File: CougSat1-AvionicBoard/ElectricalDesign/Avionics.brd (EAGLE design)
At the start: 90.4 x 95.8 mm, 214 parts, among them J1 CougSat Card, J10 IHU SD0, J11 IHU SD1, J12 IFJR SD0, J13 iFJR SD1, J14 +X Panel GPS, J15 +X, J2 -X, J3 +Z, J4 SWD, J5 +Y, J6 -Y, J7 SWD, J8 SWD, J9 -Z, U1 AD7291, U10 BNO055, U11 TXS0102DQM, U12 TXS0102DQM, U13 TXS0102DQM, U14 TXS0102DQM, U15 AD7291, U16 TXS0102DQM, U17 STM32L476RGT, U18 STM32L476RGT, U19 TXS0102DQM, U2 AD8515, U20 AD8515, U21 AD8515, U22 AD7291, U23 INA199C2, U24 AD8515, U25 DRV8837, U26 INA199C2, U27 Venus838FLPx-L, U28 DRV8837, U29 INA199C2, U3 M24M01, U30 DRV8837, U4 M24M01, U5 BNO055, U6 STM32L476RGT, U7 BNO055, U8 TXS0102DQM, U9 TXS0102DQM, Y1 32.768kHz ±10ppm, Y2 8MHz ±10ppm, Y3 32.768kHz ±10ppm, Y4 32.768kHz ±10ppm, Y5 32.768kHz ±10ppm, Y6 8MHz ±10ppm, Y7 8MHz ±10ppm, Y8 32.768kHz ±10ppm, Y9 32.768kHz ±10ppm

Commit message: Produced mCAD
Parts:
- DS1: value Yellow -> Green
- DS2: value Blue -> Green
- DS4: value Green -> Blue
- moved DS4 0.20 mm to (83.2, 4.00), flipped to the top, turned to 0 degrees
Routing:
- net 3.3V_2: track 466.7 -> 467.5 mm, vias 43 -> 44
- net GPS_LED_DIODE: track 3.69 -> 4.33 mm, vias 0 -> 1
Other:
- board text added: "Avionics V1.3"
- board text removed: "Avionics V1.1"

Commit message: new avionics update
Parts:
- added U$1: Orion B16, CougsInSpace-Boards:ORION_B16
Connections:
- new net VCC: U$1.23
- net DGND: now also U$1.10, U$1.12, U$1.13, U$1.22, U$1.24
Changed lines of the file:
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@@
 <?xml version="1.0" encoding="utf-8"?>
 <!DOCTYPE eagle SYSTEM "eagle.dtd">
-<eagle version="9.5.1">
+<eagle version="9.6.2">
 <drawing>
 <settings>
-<setting alwaysvectorfont="yes"/>
+<setting alwaysvectorfont="no"/>
 <setting verticaltext="up"/>
 </settings>
@@
 <layer number="21" name="tPlace" color="7" fill="1" visible="yes" active="yes"/>
 <layer number="22" name="bPlace" color="7" fill="1" visible="no" active="yes"/>
-<layer number="23" name="tOrigins" color="15" fill="1" visible="no" active="yes"/>
-<layer number="24" name="bOrigins" color="15" fill="1" visible="no" active="yes"/>
+<layer number="23" name="tOrigins" color="15" fill="1" visible="yes" active="yes"/>
+<layer number="24" name="bOrigins" color="15" fill="1" visible="yes" active="yes"/>
 <layer number="25" name="tNames" color="7" fill="1" visible="yes" active="yes"/>
 <layer number="26" name="bNames" color="7" fill="1" visible="no" active="yes"/>
@@
 </element>
 <element name="LOGO1" library="CougsInSpace-Aesthetics" package="SIGN-GABE" value="SIGNATUREGABE" x="87.3" y="-42.2" smashed="yes" rot="MR90"/>
+<element name="U$1" library="CougsInSpace-Boards" package="ORION_B16" value="Orion B16" x="59.6" y="-2" smashed="yes">
+<attribute name="NAME" x="59.6" y="7.1" size="0.8" layer="25" font="vector" ratio="15" align="center"/>
+<attribute name="SKU" value="03-0002" x="59.6" y="-2" size="1.778" layer="27" display="off"/>
+</element>
 </elements>
 <signals>
@@
 <wire x1="57.19" y1="-0.05" x2="55.95" y2="-1.29" width="0.2" layer="16"/>
 <wire x1="54.64" y1="-0.05" x2="54.4" y2="-0.05" width="0.2" layer="16"/>
-<wire x1="55.95" y1="-1.29" x2="55.95" y2="-1.36" width="0.2" layer="16"/>
-<wire x1="55.95" y1="-1.36" x2="55.95" y2="-1.4" width="0.2" layer="16"/>
+<wire x1="55.95" y1="-1.29" x2="55.95" y2="-1.4" width="0.2" layer="16"/>
 <via x="55.3" y="-0.89" extent="1-16" drill="0.3"/>
 <via x="52.8" y="-4.31" extent="1-16" drill="0.3"/>
@@
 <wire x1="50" y1="0" x2="55" y2="0" width="0.2" layer="2"/>
 <wire x1="55" y1="0" x2="55.3" y2="0" width="0.2" layer="2"/>
-<wire x1="55.3" y1="0" x2="55.9" y2="0" width="0.2" layer="2"/>
-<wire x1="55.9" y1="0" x2="60" y2="0" width="0.2" layer="2"/>
+<wire x1="55.3" y1="0" x2="60" y2="0" width="0.2" layer="2"/>
 <wire x1="60" y1="0" x2="65" y2="0" width="0.2" layer="2"/>
 <wire x1="65" y1="0" x2="70" y2="0" width="0.2" layer="2"/>
@@
 <wire x1="65" y1="5" x2="65" y2="10" width="0.2" layer="2"/>
 <wire x1="65" y1="10" x2="65" y2="14" width="0.2" layer="2"/>
-<wire x1="65" y1="14" x2="65" y2="16.7" width="0.2" layer="2"/>
-<wire x1="65" y1="16.7" x2="65" y2="17.9" width="0.2" layer="2"/>
+<wire x1="65" y1="14" x2="65" y2="17.9" width="0.2" layer="2"/>
 <wire x1="65" y1="17.9" x2="65" y2="21.9" width="0.2" layer="2"/>
 <wire x1="65" y1="21.9" x2="65" y2="24.9" width="0.2" layer="2"/>
@@
 <wire x1="23.835" y1="1.035" x2="23.8" y2="1" width="0.2" layer="2"/>
 <wire x1="17.6" y1="-12.9" x2="26.315" y2="-12.9" width="0.2" layer="2"/>
-<wire x1="33.62098125" y1="-12.37901875" x2="33.62098125" y2="-12.3" width="0.2" layer="2"/>
-<wire x1="33.62098125" y1="-12.3" x2="33.62098125" y2="-7.87901875" width="0.2" layer="2"/>
+<wire x1="33.62098125" y1="-12.37901875" x2="33.62098125" y2="-7.87901875" width="0.2" layer="2"/>
 <wire x1="35.5" y1="-6" x2="35.5" y2="-3.4" width="0.2" layer="2"/>
 <wire x1="33.62098125" y1="-7.87901875" x2="35.5" y2="-6" width="0.2" layer="2"/>
@@
 <wire x1="30" y1="22.505" x2="30.15" y2="22.355" width="0.2" layer="2"/>
 <wire x1="30" y1="10" x2="30" y2="11.8" width="0.2" layer="2"/>
-<wire x1="30" y1="11.8" x2="30" y2="12" width="0.2" layer="2"/>
-<wire x1="30" y1="12" x2="30" y2="13.8" width="0.2" layer="2"/>
+<wire x1="30" y1="11.8" x2="30" y2="13.8" width="0.2" layer="2"/>
 <wire x1="30" y1="13.8" x2="30" y2="22.205" width="0.2" layer="2"/>
 <wire x1="30" y1="22.205" x2="30.15" y2="22.355" width="0.2" layer="2"/>
@@
 <wire x1="35" y1="18.9" x2="35" y2="23.4" width="0.2" layer="2"/>
 <wire x1="35" y1="23.4" x2="34.7" y2="23.7" width="0.2" layer="2"/>
-<wire x1="35.465" y1="18.9" x2="35.1" y2="18.9" width="0.2" layer="2"/>
-<wire x1="35.1" y1="18.9" x2="35" y2="18.9" width="0.2" layer="2"/>
+<wire x1="35.465" y1="18.9" x2="35" y2="18.9" width="0.2" layer="2"/>
 <wire x1="34.135" y1="15.025" x2="34.975" y2="15.025" width="0.2" layer="2"/>
 <wire x1="34.975" y1="15.025" x2="35" y2="15" width="0.2" layer="2"/>
@@
 <wire x1="45" y1="14.7" x2="44.7" y2="15" width="0.2" layer="2"/>
 <wire x1="44.7" y1="15" x2="44.5" y2="15.2" width="0.2" layer="2"/>
-<wire x1="44.5" y1="17.3" x2="44.5" y2="15.2" width="0.2" layer="2"/>
 <wire x1="45.438625" y1="20.63" x2="45.13" y2="20.63" width="0.2" layer="2"/>
-<wire x1="44.5" y1="20" x2="44.5" y2="17.3" width="0.2" layer="2"/>
+<wire x1="44.5" y1="20" x2="44.5" y2="15.2" width="0.2" layer="2"/>
 <wire x1="45.13" y1="20.63" x2="44.5" y2="20" width="0.2" layer="2"/>
 <wire x1="44.9" y1="30" x2="44.9" y2="25.5" width="0.2" layer="2"/>
@@
 <wire x1="10" y1="15" x2="10.3" y2="14.7" width="0.2" layer="2"/>
 <wire x1="10.3" y1="14.7" x2="10.3" y2="11.7" width="0.2" layer="2"/>
+<contactref element="U$1" pad="10"/>
+<contactref element="U$1" pad="12"/>
+<contactref element="U$1" pad="13"/>
+<contactref element="U$1" pad="24"/>
+<contactref element="U$1" pad="22"/>
+<wire x1="53.5" y1="-6.8" x2="53.5" y2="-9" width="0" layer="19" extent="1-1"/>
+<wire x1="53.5" y1="5" x2="53.5" y2="-6.8" width="0" layer="19" extent="1-1"/>
+<wire x1="65.7" y1="5" x2="53.5" y2="5" width="0" layer="19" extent="1-1"/>
+<wire x1="65.7" y1="2.8" x2="65.7" y2="5" width="0" layer="19" extent="1-1"/>
+<wire x1="6.5" y1="-34.1" x2="65.7" y2="5" width="0" layer="19" extent="1-16"/>
 </signal>
 <signal name="AGND" class="1">
@@
 <wire x1="86.71" y1="19.86" x2="86.75" y2="19.9" width="0.2" layer="16"/>
 </signal>
+<signal name="VCC">
+<contactref element="U$1" pad="23"/>
+</signal>
 </signals>

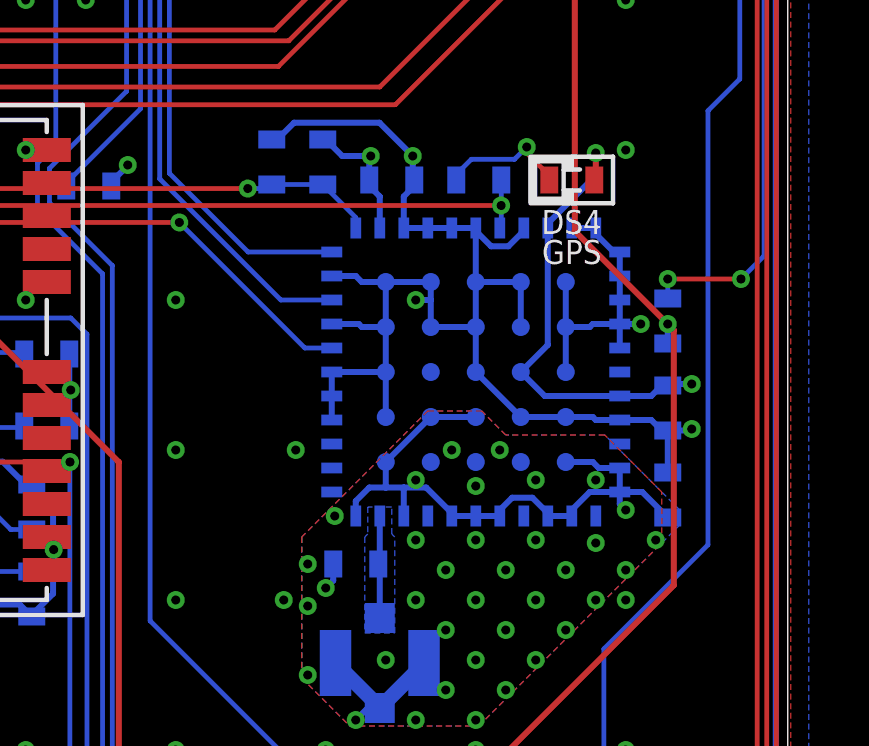
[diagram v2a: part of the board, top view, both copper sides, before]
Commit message: Added Orion B16
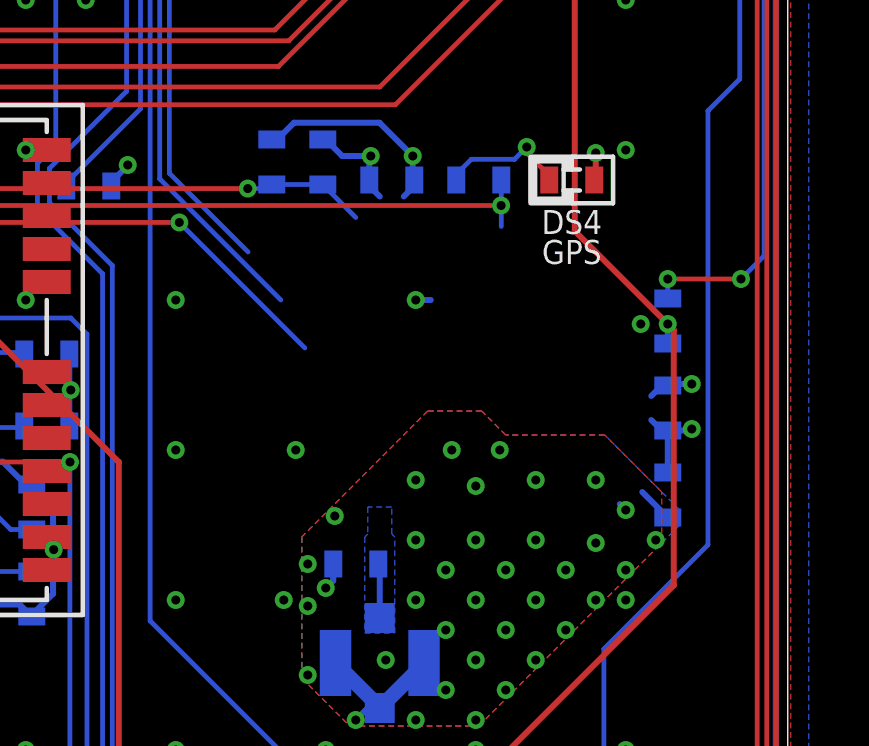
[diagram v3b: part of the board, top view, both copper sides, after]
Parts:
- removed U27: Venus838FLPx-L, CougsInSpace-RF:VENUS-1010
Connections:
- removed net VCC: U$1.23
- net !GPS_RESET: now also U$1.8; no longer U27.1
- net 3.3V_2: now also U$1.22, U$1.23; no longer U27.18, U27.2, U27.58, U27.9
- net DGND: no longer U$1.22, U27.10, U27.11, U27.12, U27.13, U27.14, U27.15, U27.16, U27.19, U27.3, U27.37, U27.38, U27.39, U27.4, U27.41, U27.43, U27.45, U27.46, U27.47, U27.48, U27.49, U27.5, U27.50, U27.51, U27.52, U27.53, U27.54, U27.55, U27.57, U27.59, U27.6, U27.60, U27.63, U27.64, U27.8
- net GPS_LED: no longer U27.7
- net GPS_PULSE: now also U$1.3; no longer U27.40
- net GPS_RFIN: now also U$1.11; no longer U27.32
- net GPS_RX: now also U$1.21; no longer U27.44
- net GPS_TX: now also U$1.20; no longer U27.42
- net RFGND: no longer U27.21, U27.22, U27.24, U27.25, U27.27, U27.28, U27.29, U27.31, U27.33, U27.61, U27.62, U27.65, U27.69
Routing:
- net DGND: track 1507.0 -> 1460.0 mm
- net RFGND: track 87.5 -> 67.2 mm
- net 3.3V_2: track 467.5 -> 454.6 mm
- net GPS_RX: track 49.8 -> 47.0 mm
- net GPS_TX: track 50.2 -> 48.5 mm
- net GPS_RFIN: track 3.44 -> 1.89 mm
- net GPS_PULSE: track 34.2 -> 33.3 mm

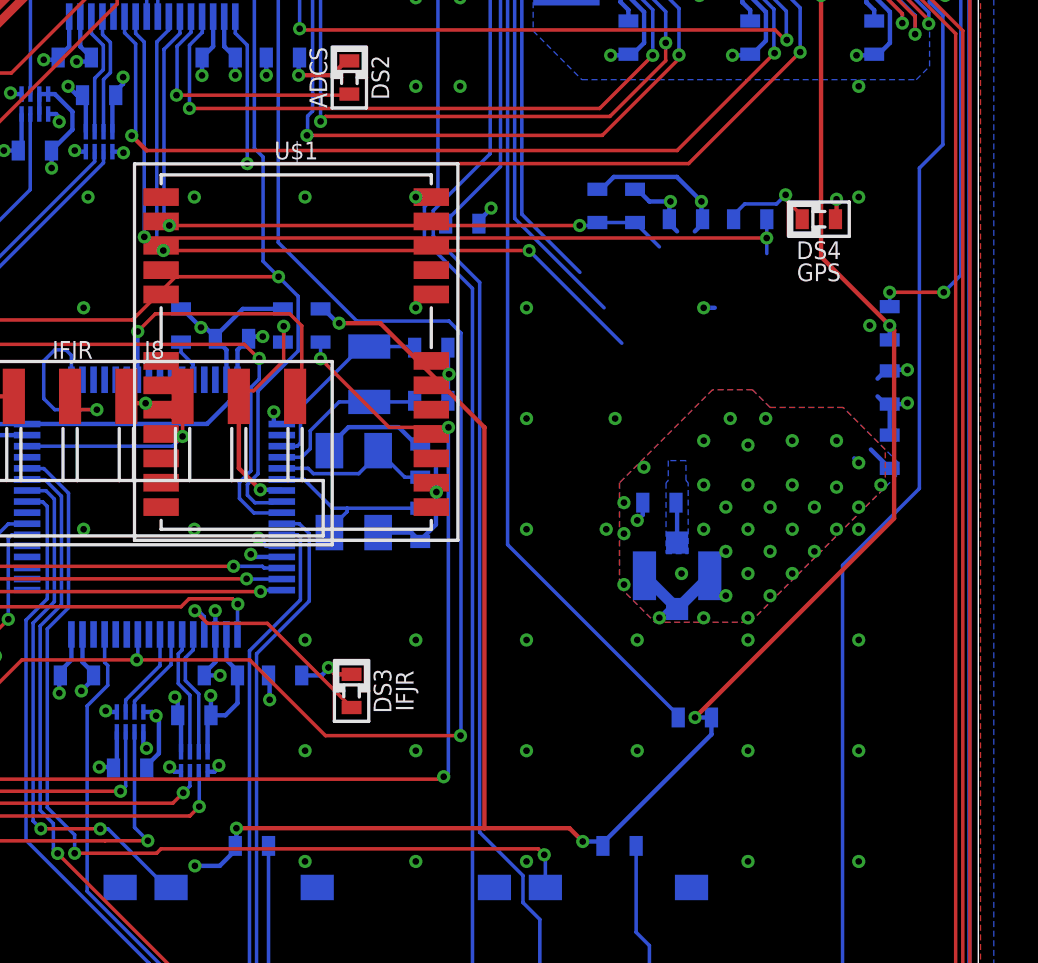
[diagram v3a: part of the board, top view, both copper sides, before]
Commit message: added Orion in brd layout
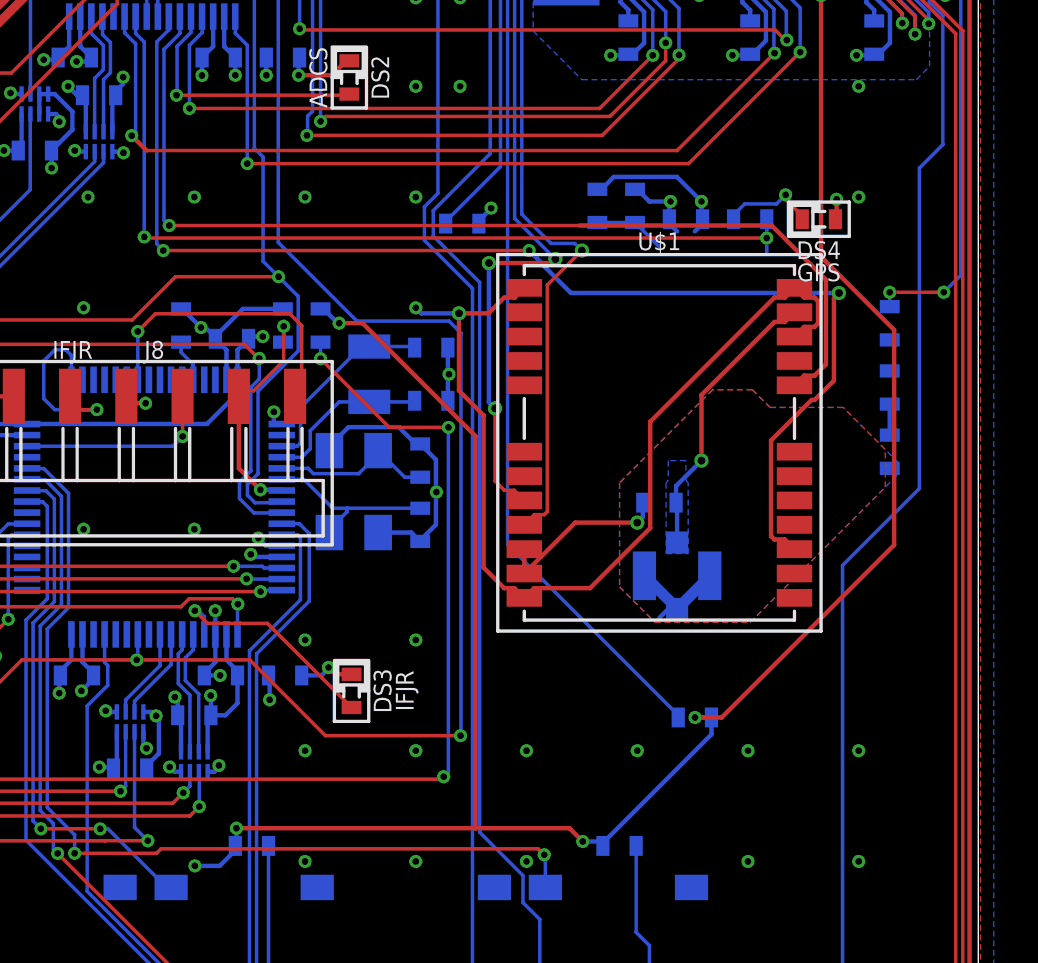
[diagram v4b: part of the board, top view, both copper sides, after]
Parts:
- moved U$1 16.9 mm to (76.0, -6.10)
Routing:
- net DGND: track 1460.0 -> 1502.5 mm, vias 237 -> 225
- net GPS_PULSE: track 33.3 -> 55.9 mm, vias 2 -> 3
- net !GPS_RESET: track 32.5 -> 50.2 mm, vias 2 -> 1
- net GPS_RX: track 47.0 -> 60.4 mm, vias 2 -> 3
- net GPS_TX: track 48.5 -> 60.1 mm, vias 2 -> 5
- net GPS_RFIN: track 1.89 -> 13.0 mm, vias 0 -> 1
- net 3.3V_2: track 454.6 -> 460.6 mm, vias 44 -> 43
- net RFGND: track 67.2 -> 65.7 mm, vias 35 -> 0
- net AGND: track 402.1 -> 401.5 mm, vias 37 -> 36
